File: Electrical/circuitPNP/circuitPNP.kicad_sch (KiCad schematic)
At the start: 85 parts, among them J1 USB_C_Receptacle_USB2.0_16P, J10 Conn_01x02_Pin, J11 Conn_01x02_Pin, J12 Conn_01x02_Pin, J13 Conn_01x02_Pin, J14 Conn_01x02_Pin, J15 Conn_01x02_Pin, J16 Conn_01x02_Pin, J17 Conn_01x02_Pin, J18 Conn_01x02_Pin, J19 Conn_01x02_Pin, J2 Screw_Terminal_01x02, J20 Conn_01x02_Pin, J21 Conn_01x04_Pin, J22 Conn_01x04_Pin, J23 Conn_01x04_Pin, J24 Conn_01x04_Pin, J25 Conn_01x04_Pin, J26 Conn_01x02_Pin, J27 Conn_01x02_Pin, J28 Conn_01x04_Pin, J3 Screw_Terminal_01x02, J4 Conn_01x02_Pin, J5 Conn_01x02_Pin, J6 Conn_01x02_Pin, J7 Conn_01x02_Pin, J8 Conn_01x02_Pin, J9 Conn_01x02_Pin, Q1 GS66504B, Q2 GS66504B, SW1 SW_Push, SW2 SW_Push, SW3 SW_Slide_DPDT, U1 ESP32-S3-WROOM-1, U3 SN65HVD230, U4 AMS1117-3.3

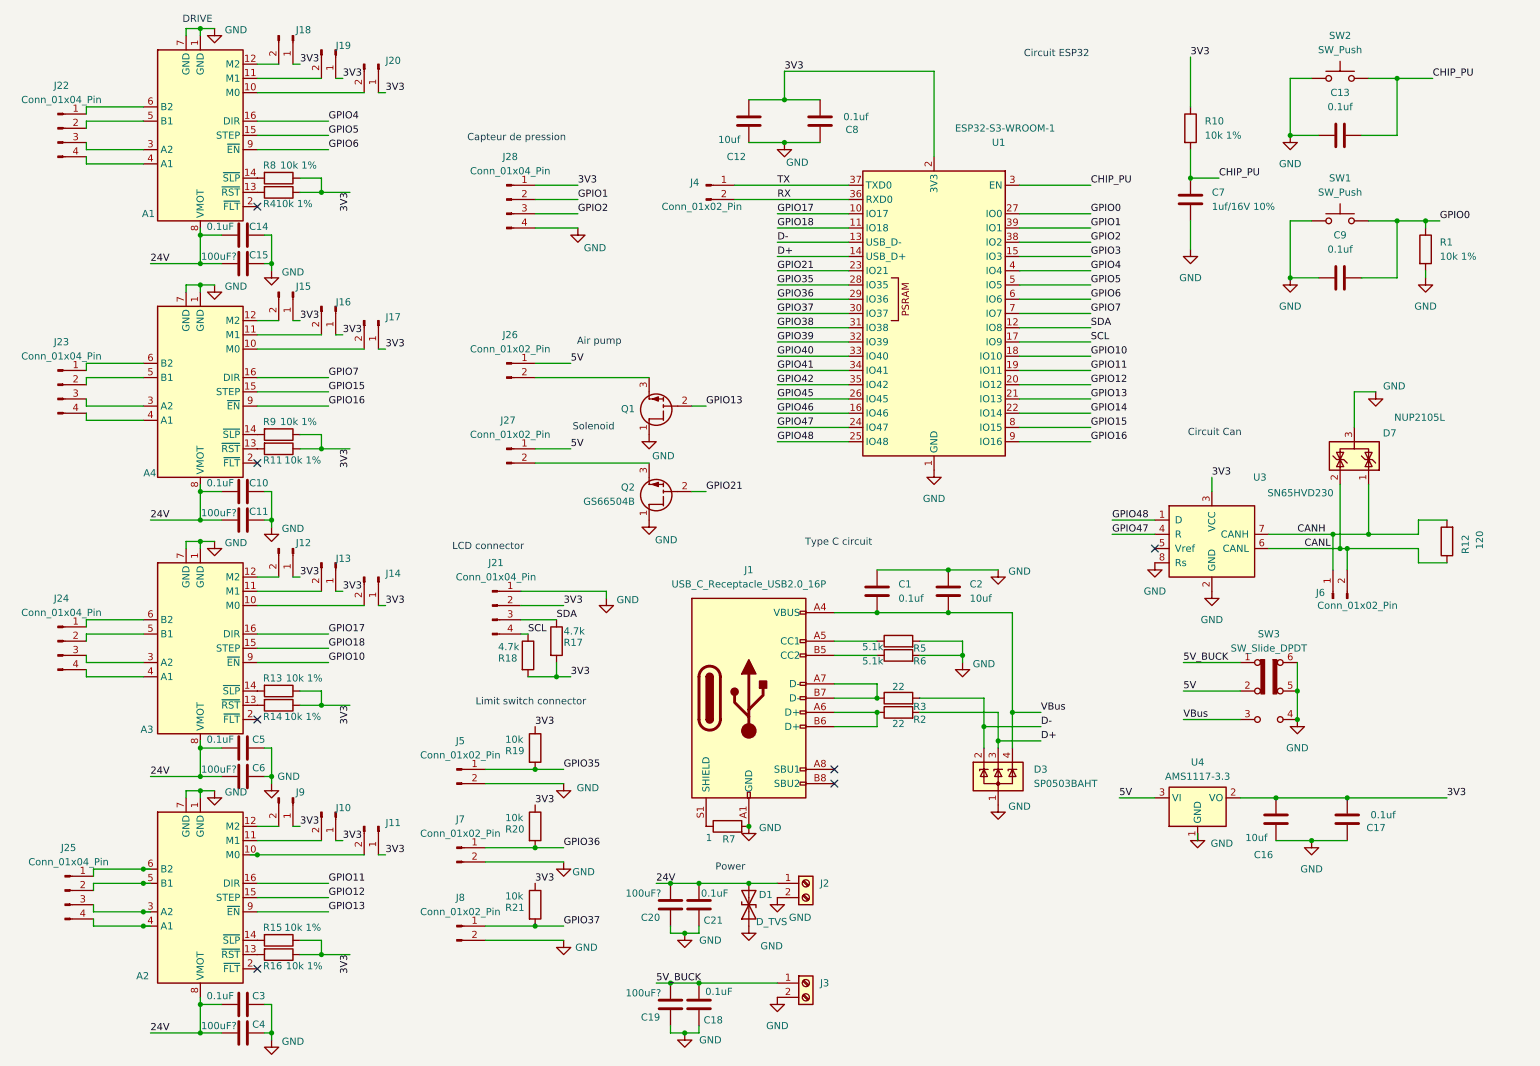
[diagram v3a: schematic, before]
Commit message: only bulck cap value missing, all footprint are selected for a pcb
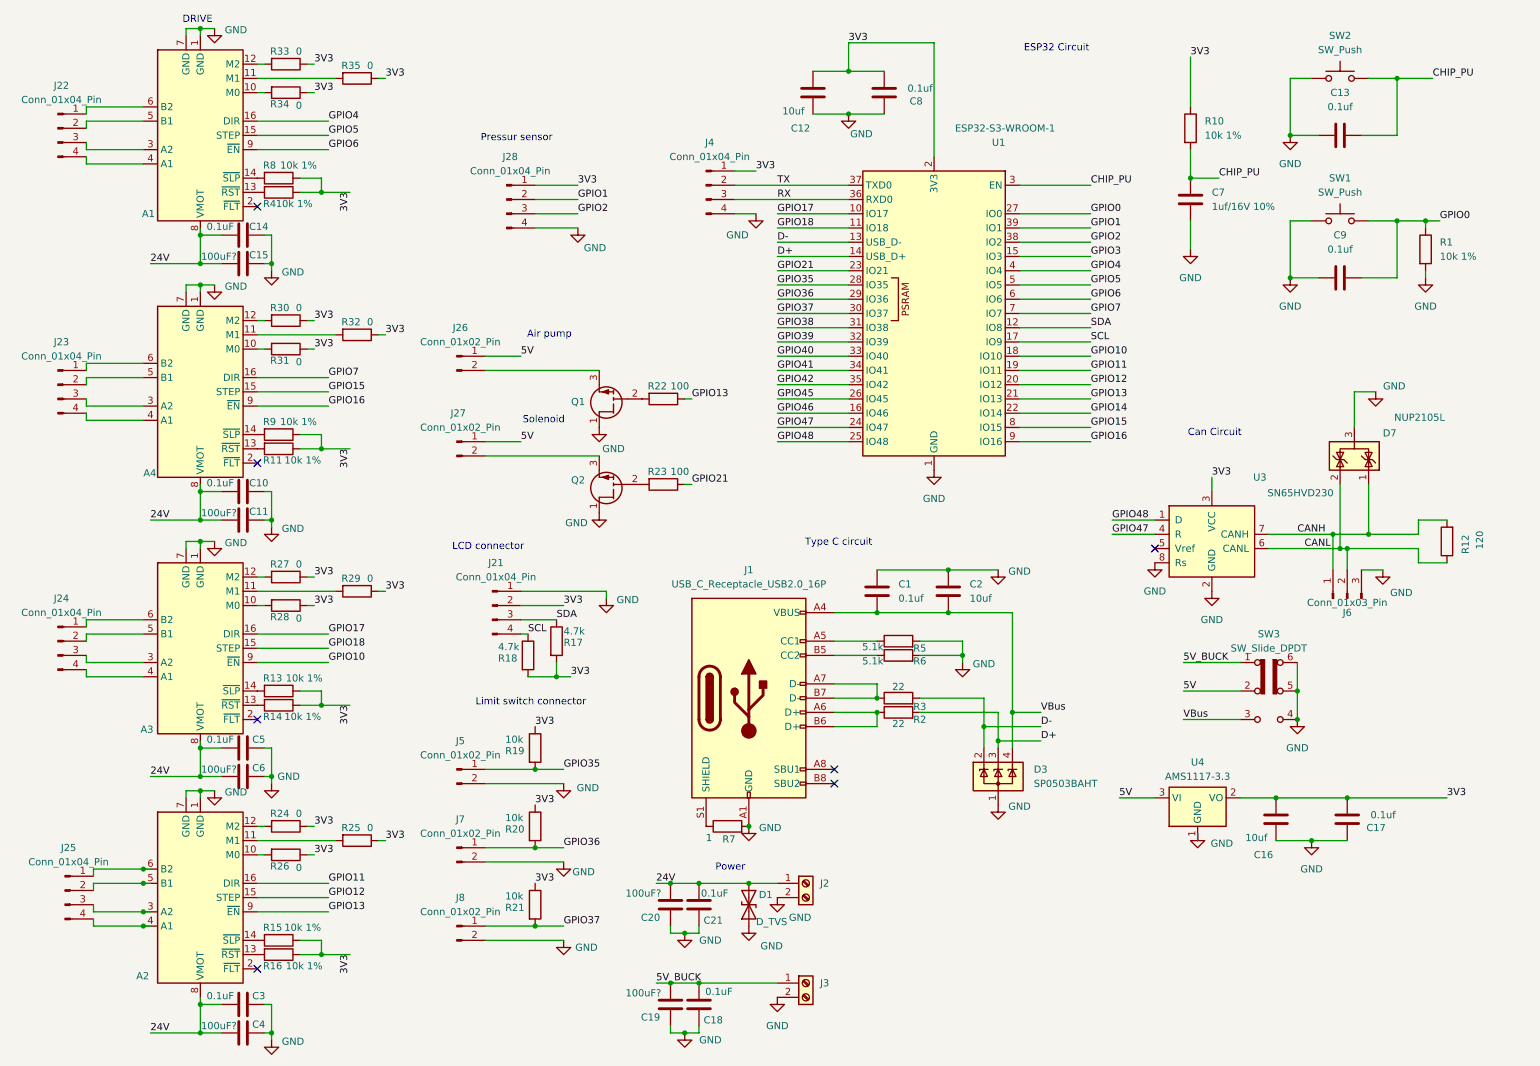
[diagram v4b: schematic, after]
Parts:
- removed J10, J11, J12, J13, J14, J15, J16, J17, J18, J19, J20, J9: Conn_01x02_Pin, symbol Connector:Conn_01x02_Pin
- removed J4: Conn_01x02_Pin, Connector_PinHeader_2.54mm:PinHeader_1x02_P2.54mm_Vertical, symbol Connector:Conn_01x02_Pin
- removed J6: Conn_01x02_Pin, Connector_Molex:Molex_KK-396_A-41792-0002_1x02_P3.96mm_Horizontal, symbol Connector:Conn_01x02_Pin
- added J4: Conn_01x04_Pin, Connector_PinSocket_2.54mm:PinSocket_1x04_P2.54mm_Vertical, symbol Connector:Conn_01x04_Pin
- added J6: Conn_01x03_Pin, Connector_Molex:Molex_KK-254_AE-6410-03A_1x03_P2.54mm_Vertical, symbol Connector:Conn_01x03_Pin
- added R22, R23: 100, Resistor_SMD:R_0603_1608Metric_Pad0.98x0.95mm_HandSolder, symbol Device:R
- added R24, R25, R26, R27, R28, R29, R30, R31, R32, R33, R34, R35: 0, Resistor_SMD:R_0603_1608Metric_Pad0.98x0.95mm_HandSolder, symbol Device:R
- C10, C14, C18, C21, C3, C5: footprint (none) -> Capacitor_SMD:C_0603_1608Metric_Pad1.08x0.95mm_HandSolder
- C11, C15, C19, C20, C4, C6: footprint (none) -> Capacitor_SMD:CP_Elec_8x10
- D1: footprint (none) -> Diode_SMD:D_SMB
- J2, J3: footprint (none) -> TerminalBlock:TerminalBlock_MaiXu_MX126-5.0-02P_1x02_P5.00mm
- J21, J22, J23, J24, J25: footprint (none) -> Connector_Molex:Molex_KK-254_AE-6410-04A_1x04_P2.54mm_Vertical
- J26, J27, J5, J7, J8: footprint (none) -> Connector_Molex:Molex_KK-254_AE-6410-02A_1x02_P2.54mm_Vertical
- J28: footprint (none) -> Connector_PinSocket_2.54mm:PinSocket_1x04_P2.54mm_Vertical
- Q1, Q2: value GS66504B -> IRLML6344TRPBF; footprint Transistor_Power:GaN_Systems_GaNPX-3_5x6.6mm_Drain3.76x0.6mm -> Package_TO_SOT_SMD:SOT-23
- SW3: footprint (none) -> SLW-1278105:SW_SLW-1678105-6A-N-D
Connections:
- net 3V3: now also J4.1 (Pin_1), R24.1, R25.1, R26.1, R27.1, R28.1, R29.1, R30.1, R31.1, R32.1, R33.1, R34.1, R35.1
- net CANH: now also J6.1 (Pin_1)
- net CANL: now also J6.2 (Pin_2)
- net GND: now also J4.4 (Pin_4), J6.3 (Pin_3)
- net GPIO13: now also R22.1; no longer Q1.2 (G)
- net GPIO21: now also R23.1; no longer Q2.2 (G)
- net RX: now also J4.3 (Pin_3)
- net TX: now also J4.2 (Pin_2)
- net at A4.12 (M2): now also R30.2
- net at A1.10 (M0): now also R34.2
- net at A1.11 (M1): now also R35.2
- net at A1.12 (M2): now also R33.2
- net at A4.10 (M0): now also R31.2
- net at A4.11 (M1): now also R32.2
- net at A3.10 (M0): now also R28.2
- net at A3.11 (M1): now also R29.2
- net at A3.12 (M2): now also R27.2
- net at A2.10 (M0): now also R26.2
- net at A2.11 (M1): now also R25.2
- net at A2.12 (M2): now also R24.2
- new net: Q2.2 (G), R23.2
- new net: Q1.2 (G), R22.2
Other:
- note added: "Can Circuit"
- note added: "ESP32 Circuit"
- note added: "Pressur sensor"
- note removed: "Capteur de pression"
- note removed: "Circuit Can"
- note removed: "Circuit ESP32"
- moved on the sheet: C12, C8, J26, J27, Q1, Q2

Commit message: circuit done
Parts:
- added C22: 10uf, Capacitor_SMD:C_0603_1608Metric_Pad1.08x0.95mm_HandSolder, symbol Device:C
- added C23: 0.1uf, Capacitor_SMD:C_0603_1608Metric_Pad1.08x0.95mm_HandSolder, symbol Device:C
- added D2, D4: D, Diode_SMD:D_SMB, symbol Device:D
- C11, C15, C19, C20, C4, C6: value 100uF? -> 100uF
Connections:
- net 5V: now also C22.2, C23.2, D2.1 (K), D4.1 (K)
- net GND: now also C22.1, C23.1
- net at J27.2 (Pin_2), Q2.3 (S): now also D4.2 (A)
- net at J26.2 (Pin_2), Q1.3 (S): now also D2.2 (A)
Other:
- moved on the sheet: C16, C17, U4

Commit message: pcb wip
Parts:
- removed C22: 10uf, Capacitor_SMD:C_0603_1608Metric_Pad1.08x0.95mm_HandSolder, symbol Device:C
- removed C23: 0.1uf, Capacitor_SMD:C_0603_1608Metric_Pad1.08x0.95mm_HandSolder, symbol Device:C
- removed J4: Conn_01x04_Pin, Connector_PinSocket_2.54mm:PinSocket_1x04_P2.54mm_Vertical, symbol Connector:Conn_01x04_Pin
- added H1, H2, H3, H4: MountingHole, MountingHole:MountingHole_3.2mm_M3, symbol Mechanical:MountingHole
- added J4: Conn_01x03_Pin, Connector_PinHeader_2.54mm:PinHeader_1x03_P2.54mm_Vertical, symbol Connector:Conn_01x03_Pin
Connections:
- net 5V_BUCK: now also SW3.3 (C); no longer SW3.1 (A)
- net CANH: now also J6.3 (Pin_3); no longer J6.1 (Pin_1)
- net GND: now also J6.1 (Pin_1), J4.3 (Pin_3); no longer J6.3 (Pin_3)
- net GPIO13: no longer A2.9 (~{EN}), R22.1
- net GPIO3: now also R22.1
- net GPIO46: now also A2.9 (~{EN})
- net RX: now also J4.2 (Pin_2)
- net TX: now also J4.1 (Pin_1)
- net VBus: now also SW3.1 (A); no longer SW3.3 (C)

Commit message: wip pcb
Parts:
- J2, J3: footprint TerminalBlock:TerminalBlock_MaiXu_MX126-5.0-02P_1x02_P5.00mm -> Connector_Molex:Molex_KK-396_A-41792-0002_1x02_P3.96mm_Horizontal
- J22, J23, J24, J25: footprint Connector_Molex:Molex_KK-254_AE-6410-04A_1x04_P2.54mm_Vertical -> Connector_Molex:Molex_KK-396_A-41792-0004_1x04_P3.96mm_Horizontal
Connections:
- net 3V3: now also R1.2
- net GND: no longer R1.2
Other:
- note added: "switch terminal for molex 396 switch drive connector for molex 396"
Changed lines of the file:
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@@
 		)
 	)
+	(text "switch terminal for molex 396\nswitch drive connector for molex 396\n"
+		(exclude_from_sim no)
+		(at 222.504 170.18 0)
+		(effects
+			(font
+				(size 1.27 1.27)
+			)
+		)
+	)
 	(junction
 		(at 66.04 102.87)
@@
 		)
 	)
+	(label "3V3"
+		(at 271.78 59.69 0)
+		(effects
+			(font
+				(size 1.27 1.27)
+			)
+			(justify left bottom)
+		)
+	)
 	(label "GPIO13"
 		(at 212.09 81.28 0)
@@
 			)
 		)
-		(property "Footprint" "TerminalBlock:TerminalBlock_MaiXu_MX126-5.0-02P_1x02_P5.00mm"
+		(property "Footprint" "Connector_Molex:Molex_KK-396_A-41792-0002_1x02_P3.96mm_Horizontal"
 			(at 161.29 185.42 0)
 			(effects
@@
 			)
 		)
-		(property "Footprint" "Connector_Molex:Molex_KK-254_AE-6410-04A_1x04_P2.54mm_Vertical"
+		(property "Footprint" "Connector_Molex:Molex_KK-396_A-41792-0004_1x04_P3.96mm_Horizontal"
 			(at 27.94 124.46 0)
 			(effects
@@
 			)
 		)
-		(property "Footprint" "Connector_Molex:Molex_KK-254_AE-6410-04A_1x04_P2.54mm_Vertical"
+		(property "Footprint" "Connector_Molex:Molex_KK-396_A-41792-0004_1x04_P3.96mm_Horizontal"
 			(at 27.94 33.02 0)
 			(effects
@@
 			)
 		)
-		(property "Footprint" "Connector_Molex:Molex_KK-254_AE-6410-04A_1x04_P2.54mm_Vertical"
+		(property "Footprint" "Connector_Molex:Molex_KK-396_A-41792-0004_1x04_P3.96mm_Horizontal"
 			(at 27.94 78.74 0)
 			(effects
@@
 	)
 	(symbol
-		(lib_id "power:GND")
-		(at 271.78 59.69 0)
-		(unit 1)
-		(exclude_from_sim no)
-		(in_bom yes)
-		(on_board yes)
-		(dnp no)
-		(fields_autoplaced yes)
-		(property "Reference" "#PWR08"
-			(at 271.78 66.04 0)
-			(effects
-				(font
-					(size 1.27 1.27)
-				)
-				(hide yes)
-			)
-		)
-		(property "Value" "GND"
-			(at 271.78 64.77 0)
-			(effects
-				(font
-					(size 1.27 1.27)
-				)
-			)
-		)
-		(property "Footprint" ""
-			(at 271.78 59.69 0)
-			(effects
-				(font
-					(size 1.27 1.27)
-				)
-				(hide yes)
-			)
-		)
-		(property "Datasheet" ""
-			(at 271.78 59.69 0)
-			(effects
-				(font
-					(size 1.27 1.27)
-				)
-				(hide yes)
-			)
-		)
-		(property "Description" "Power symbol creates a global label with name \"GND\" , ground"
-			(at 271.78 59.69 0)
-			(effects
-				(font
-					(size 1.27 1.27)
-				)
-				(hide yes)
-			)
-		)
-		(pin "1"
-		)
-		(instances
-			(project "circuitPNP"
-				(path "/cdf8736a-c168-4946-980b-ea20704015fc"
-					(reference "#PWR08")
-					(unit 1)
-				)
-			)
-		)
-	)
-	(symbol
 		(lib_id "Switch:SW_Push")
 		(at 256.54 24.13 0)
@@
 			)
 		)
-		(property "Footprint" "Connector_Molex:Molex_KK-254_AE-6410-04A_1x04_P2.54mm_Vertical"
+		(property "Footprint" "Connector_Molex:Molex_KK-396_A-41792-0004_1x04_P3.96mm_Horizontal"
 			(at 29.21 168.91 0)
 			(effects
@@
 			)
 		)
-		(property "Footprint" "TerminalBlock:TerminalBlock_MaiXu_MX126-5.0-02P_1x02_P5.00mm"
+		(property "Footprint" "Connector_Molex:Molex_KK-396_A-41792-0002_1x02_P3.96mm_Horizontal"
 			(at 161.29 167.64 0)
 			(effects

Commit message: pcb done, wainting for circuit testing
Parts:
- added D5, D6: LED, LED_SMD:LED_0603_1608Metric, symbol Device:LED
- added R36, R37: 330, Resistor_SMD:R_0603_1608Metric_Pad0.98x0.95mm_HandSolder, symbol Device:R
- added TP1, TP2, TP3, TP4, TP5, TP6, TP7, TP8: TestPoint, TestPoint:TestPoint_Pad_D2.0mm, symbol Connector:TestPoint
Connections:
- net 24V: now also TP1.1
- net 3V3: now also R37.1, TP8.1
- net 5V: no longer D2.1 (K), D4.1 (K), J26.1 (Pin_1), J27.1 (Pin_1)
- net 5V_BUCK: now also D2.1 (K), D4.1 (K), J26.1 (Pin_1), J27.1 (Pin_1), TP3.1
- net CHIP_PU: now also TP5.1
- net GND: now also D5.1 (K), D6.1 (K), TP6.1, TP7.1; no longer SW3.4 (A), SW3.5 (B), SW3.6 (C)
- net GPIO0: now also TP4.1
- net GPIO10: now also R36.1; no longer A3.9 (~{EN})
- net GPIO11: now also A2.9 (~{EN}); no longer A2.16 (DIR)
- net GPIO12: now also A1.16 (DIR); no longer A2.15 (STEP)
- net GPIO13: now also A1.15 (STEP)
- net GPIO14: now also A1.9 (~{EN})
- net GPIO15: now also A4.9 (~{EN}); no longer A4.15 (STEP)
- net GPIO16: now also A3.16 (DIR); no longer A4.9 (~{EN})
- net GPIO17: now also A3.15 (STEP); no longer A3.16 (DIR)
- net GPIO18: now also A3.9 (~{EN}); no longer A3.15 (STEP)
- net GPIO21: no longer R23.1
- net GPIO3: now also A2.16 (DIR); no longer R22.1
- net GPIO4: now also R23.1; no longer A1.16 (DIR)
- net GPIO46: now also A2.15 (STEP); no longer A2.9 (~{EN})
- net GPIO5: now also R22.1; no longer A1.15 (STEP)
- net GPIO6: now also A4.16 (DIR); no longer A1.9 (~{EN})
- net GPIO7: now also A4.15 (STEP); no longer A4.16 (DIR)
- net VBus: now also TP2.1
- new net: D5.2 (A), R36.2
- new net: D6.2 (A), R37.2
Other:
- note added: "Built in LED"
- moved on the sheet: D2, D4, J26, J27, Q1, Q2, R22, R23
